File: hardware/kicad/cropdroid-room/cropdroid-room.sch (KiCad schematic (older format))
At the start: 42 parts, among them CON1 SJ1-3523N, CON2 SJ1-3523N, CON3 SJ1-3523N, CON4 SJ1-3523N, J1 OSTTC020162, J2 PJ-102A, J3 OSTTC020162, J4 OSTTC020162, J5 OSTTC020162, J6 OSTTC020162, J7 640456-3, J8 640456-3, J9 640456-3, K1 T9AS1D12-15, K2 T9AS1D12-15, K3 T9AS1D12-15, K4 T9AS1D12-15, K5 T9AS1D12-15, Q1 ULN2003AN, U1 PPTC151LFBN-RC, U2 PPTC151LFBN-RC

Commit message: finalize prototype v0.1a
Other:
- note added: "Channel 0"
- note added: "Channel 1"
- note added: "Channel 2"
- note added: "Channel 3"
- note added: "Channel 4"
- note added: "DHT22\nBottom"
- note added: "DHT22\nCanopy"
- note added: "DHT22\nTop"
- note removed: "A/C"
- note removed: "Dehumidifier"
- note removed: "Heater"
- note removed: "Lighting"
- note removed: "Ventiliation"
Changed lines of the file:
@@
 	0    -1   -1   0
 $EndComp
-Text Notes 4100 7300 0    50   ~ 0
-A/C
-Text Notes 5200 7300 0    50   ~ 0
-Heater
+Text Notes 4000 7300 0    50   ~ 0
+Channel 1
+Text Notes 5100 7300 0    50   ~ 0
+Channel 2
 Text Notes 6100 7300 0    50   ~ 0
-Dehumidifier
+Channel 3
 Text Notes 7150 7300 0    50   ~ 0
-Ventiliation
+Channel 4
 $Comp
 L Device:LED D4
@@
 	2900 8300 3950 8300
 Connection ~ 3950 8300
-Text Notes 3000 7300 0    50   ~ 0
-Lighting
+Text Notes 2950 7300 0    50   ~ 0
+Channel 0
 Connection ~ 4650 5450
 Wire Wire Line
@@
 EndData
 $EndBitmap
+Text Notes 10500 2300 0    50   ~ 0
+DHT22\nTop
+Text Notes 11550 2300 0    50   ~ 0
+DHT22\nCanopy
+Text Notes 12600 2300 0    50   ~ 0
+DHT22\nBottom
 $EndSCHEMATC

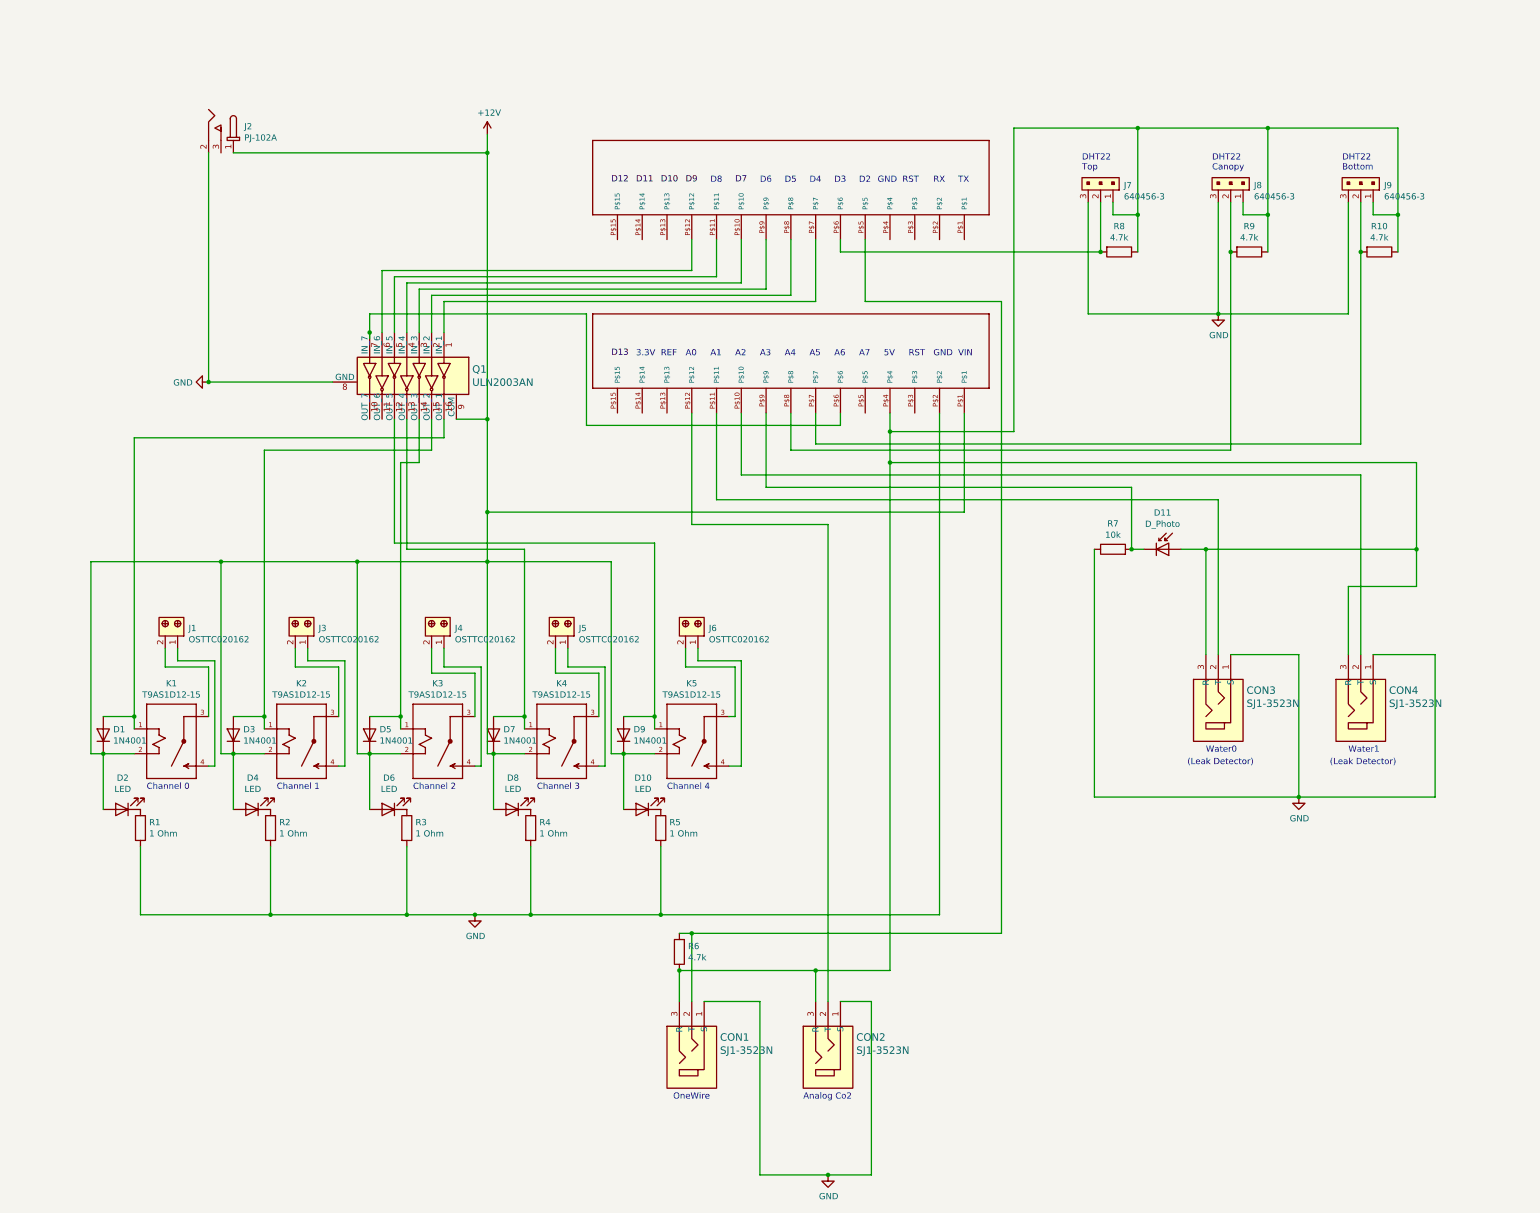
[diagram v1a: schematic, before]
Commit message: upgrade hardware to v0.2a (120v)
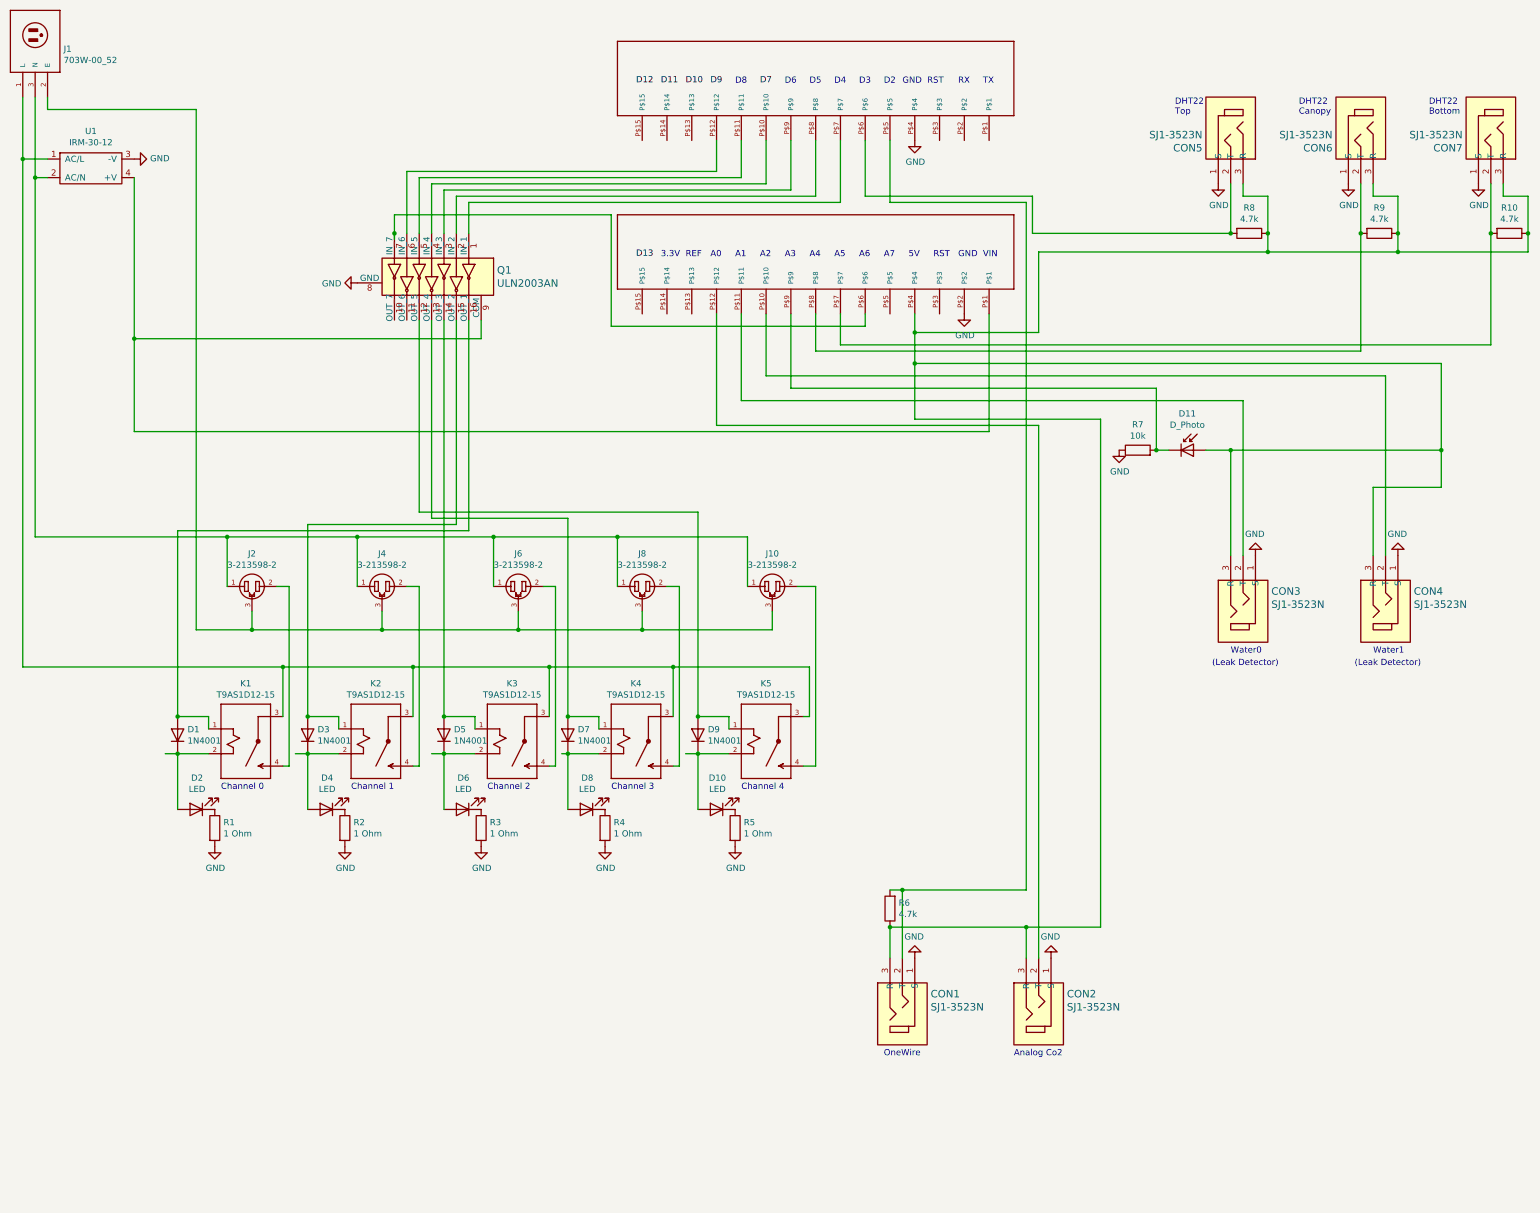
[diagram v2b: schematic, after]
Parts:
- removed J1, J3, J4, J5, J6: OSTTC020162, digikey-footprints:Term_Block_1x2_P5mm, symbol dk_Terminal-Blocks-Wire-to-Board:OSTTC020162
- removed J2: PJ-102A, digikey-footprints:Barrel_Jack_5.5mmODx2.1mmID_PJ-102A, symbol dk_Barrel-Power-Connectors:PJ-102A
- removed J7, J8, J9: 640456-3, digikey-footprints:PinHeader_1x3_P2.54_Drill1.1mm, symbol dk_Rectangular-Connectors-Headers-Male-Pins:640456-3
- added CON5, CON6, CON7: SJ1-3523N, digikey-footprints:Headphone_Jack_3.5mm_SJ1-3523N, symbol dk_Barrel-Audio-Connectors:SJ1-3523N
- added J1: 703W-00_52, 703W-00_52:52, symbol 703W-00_52:703W-00_52
- added J10, J2, J4, J6, J8: 3-213598-2, 3-213598-2:TE_3-213598-2, symbol 3-213598-2:3-213598-2
- added U1: IRM-30-12, IRM-30-12:IRM-30-12, symbol IRM-30-12:IRM-30-12
- renumbered U1 to U2, U2 to U3
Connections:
- net labels removed: +12V
- wire segments 211 -> 189
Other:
- moved on the sheet: CON1, CON2, CON3, CON4, D1, D10, D11, D2, D3, D4, D5, D6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

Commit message: final kicad v0.2a
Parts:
- renumbered CON5 to CON3, CON3 to CON4, CON6 to CON5, CON4 to CON6, J4 to J3, J6 to J4, J8 to J5, J10 to J6
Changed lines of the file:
@@
 	13800 2400 13800 2800
 $Comp
-L power:GND #PWR011
+L power:GND #PWR013
 U 1 1 5E3D3C7D
 P 11600 2400
-F 0 "#PWR011" H 11600 2150 50  0001 C CNN
+F 0 "#PWR013" H 11600 2150 50  0001 C CNN
 F 1 "GND" H 11605 2227 50  0000 C CNN
 F 2 "" H 11600 2400 50  0001 C CNN
@@
 $EndComp
 $Comp
-L 3-213598-2:3-213598-2 J4
+L 3-213598-2:3-213598-2 J3
 U 1 1 5E6963C0
 P 4850 5650
-F 0 "J4" H 4850 5915 50  0000 C CNN
+F 0 "J3" H 4850 5915 50  0000 C CNN
 F 1 "3-213598-2" H 4850 5824 50  0000 C CNN
 F 2 "3-213598-2:TE_3-213598-2" H 4850 5650 50  0001 L BNN
@@
 $EndComp
 $Comp
-L 3-213598-2:3-213598-2 J6
+L 3-213598-2:3-213598-2 J4
 U 1 1 5E6B11C9
 P 5950 5650
-F 0 "J6" H 5950 5915 50  0000 C CNN
+F 0 "J4" H 5950 5915 50  0000 C CNN
 F 1 "3-213598-2" H 5950 5824 50  0000 C CNN
 F 2 "3-213598-2:TE_3-213598-2" H 5950 5650 50  0001 L BNN
@@
 $EndComp
 $Comp
-L 3-213598-2:3-213598-2 J8
+L 3-213598-2:3-213598-2 J5
 U 1 1 5E6B3BE3
 P 6950 5650
-F 0 "J8" H 6950 5915 50  0000 C CNN
+F 0 "J5" H 6950 5915 50  0000 C CNN
 F 1 "3-213598-2" H 6950 5824 50  0000 C CNN
 F 2 "3-213598-2:TE_3-213598-2" H 6950 5650 50  0001 L BNN
@@
 $EndComp
 $Comp
-L 3-213598-2:3-213598-2 J10
+L 3-213598-2:3-213598-2 J6
 U 1 1 5E6B4B70
 P 8000 5650
-F 0 "J10" H 8000 5915 50  0000 C CNN
+F 0 "J6" H 8000 5915 50  0000 C CNN
 F 1 "3-213598-2" H 8000 5824 50  0000 C CNN
 F 2 "3-213598-2:TE_3-213598-2" H 8000 5650 50  0001 L BNN
@@
 $EndComp
 $Comp
-L power:GND #PWR09
+L power:GND #PWR010
 U 1 1 5E68B170
 P 9550 3450
-F 0 "#PWR09" H 9550 3200 50  0001 C CNN
+F 0 "#PWR010" H 9550 3200 50  0001 C CNN
 F 1 "GND" H 9555 3277 50  0000 C CNN
 F 2 "" H 9550 3450 50  0001 C CNN
@@
 	9150 3450 9150 3600
 $Comp
-L dk_Barrel-Audio-Connectors:SJ1-3523N CON4
+L dk_Barrel-Audio-Connectors:SJ1-3523N CON6
 U 1 1 5E3F89E9
 P 12950 5800
-F 0 "CON4" V 13061 5572 60  0000 R CNN
+F 0 "CON6" V 13061 5572 60  0000 R CNN
 F 1 "SJ1-3523N" V 12955 5572 60  0000 R CNN
 F 2 "digikey-footprints:Headphone_Jack_3.5mm_SJ1-3523N" H 13150 6000 60  0001 L CNN
@@
 	9750 3450 9750 4400
 $Comp
-L dk_Barrel-Audio-Connectors:SJ1-3523N CON5
+L dk_Barrel-Audio-Connectors:SJ1-3523N CON3
 U 1 1 5E43B38C
 P 11700 2000
-F 0 "CON5" V 11811 1772 60  0000 R CNN
+F 0 "CON3" V 11811 1772 60  0000 R CNN
 F 1 "SJ1-3523N" V 11705 1772 60  0000 R CNN
 F 2 "digikey-footprints:Headphone_Jack_3.5mm_SJ1-3523N" H 11900 2200 60  0001 L CNN
@@
 $EndComp
 $Comp
-L dk_Barrel-Audio-Connectors:SJ1-3523N CON6
+L dk_Barrel-Audio-Connectors:SJ1-3523N CON5
 U 1 1 5E43C0EF
 P 12750 2000
-F 0 "CON6" V 12861 1772 60  0000 R CNN
+F 0 "CON5" V 12861 1772 60  0000 R CNN
 F 1 "SJ1-3523N" V 12755 1772 60  0000 R CNN
 F 2 "digikey-footprints:Headphone_Jack_3.5mm_SJ1-3523N" H 12950 2200 60  0001 L CNN
@@
 	13050 2950 14100 2950
 $Comp
-L power:GND #PWR0101
+L power:GND #PWR015
 U 1 1 5E5124F0
 P 12650 2400
-F 0 "#PWR0101" H 12650 2150 50  0001 C CNN
+F 0 "#PWR015" H 12650 2150 50  0001 C CNN
 F 1 "GND" H 12655 2227 50  0000 C CNN
 F 2 "" H 12650 2400 50  0001 C CNN
@@
 $EndComp
 $Comp
-L power:GND #PWR0102
+L power:GND #PWR017
 U 1 1 5E5128D5
 P 13700 2400
-F 0 "#PWR0102" H 13700 2150 50  0001 C CNN
+F 0 "#PWR017" H 13700 2150 50  0001 C CNN
 F 1 "GND" H 13705 2227 50  0000 C CNN
 F 2 "" H 13700 2400 50  0001 C CNN
@@
 Connection ~ 12000 2950
 $Comp
-L power:GND #PWR0104
+L power:GND #PWR014
 U 1 1 5E5E6FDB
 P 11900 5400
-F 0 "#PWR0104" H 11900 5150 50  0001 C CNN
+F 0 "#PWR014" H 11900 5150 50  0001 C CNN
 F 1 "GND" H 11905 5227 50  0000 C CNN
 F 2 "" H 11900 5400 50  0001 C CNN
@@
 $EndComp
 $Comp
-L power:GND #PWR0105
+L power:GND #PWR016
 U 1 1 5E5E7854
 P 13050 5400
-F 0 "#PWR0105" H 13050 5150 50  0001 C CNN
+F 0 "#PWR016" H 13050 5150 50  0001 C CNN
 F 1 "GND" H 13055 5227 50  0000 C CNN
 F 2 "" H 13050 5400 50  0001 C CNN
@@
 $EndComp
 $Comp
-L dk_Barrel-Audio-Connectors:SJ1-3523N CON3
+L dk_Barrel-Audio-Connectors:SJ1-3523N CON4
 U 1 1 5E395223
 P 11800 5800
-F 0 "CON3" V 11911 5572 60  0000 R CNN
+F 0 "CON4" V 11911 5572 60  0000 R CNN
 F 1 "SJ1-3523N" V 11805 5572 60  0000 R CNN
 F 2 "digikey-footprints:Headphone_Jack_3.5mm_SJ1-3523N" H 12000 6000 60  0001 L CNN
@@
 	10650 4300 9150 4300
 $Comp
-L power:GND #PWR?
+L power:GND #PWR09
 U 1 1 5E5D8888
 P 9150 8650
-F 0 "#PWR?" H 9150 8400 50  0001 C CNN
+F 0 "#PWR09" H 9150 8400 50  0001 C CNN
 F 1 "GND" H 9155 8477 50  0000 C CNN
 F 2 "" H 9150 8650 50  0001 C CNN
@@
 $EndComp
 $Comp
-L power:GND #PWR010
+L power:GND #PWR011
 U 1 1 5EB22757
 P 10250 8650
-F 0 "#PWR010" H 10250 8400 50  0001 C CNN
+F 0 "#PWR011" H 10250 8400 50  0001 C CNN
 F 1 "GND" H 10255 8477 50  0000 C CNN
 F 2 "" H 10250 8650 50  0001 C CNN
